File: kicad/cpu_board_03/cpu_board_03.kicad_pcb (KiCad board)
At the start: 2 copper layers, 99.1 x 94.2 mm, 62 parts, among them J1 DIN41612_02x32_AC, J11 Conn_01x09, J2 Clock, J6 Conn_01x02_Socket, J9 Ram1 Enable, SW1 SW_Reset, SW2 SW_PWR, U1 W65C02SxP, U10 74HC245, U13 74AHC1G32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

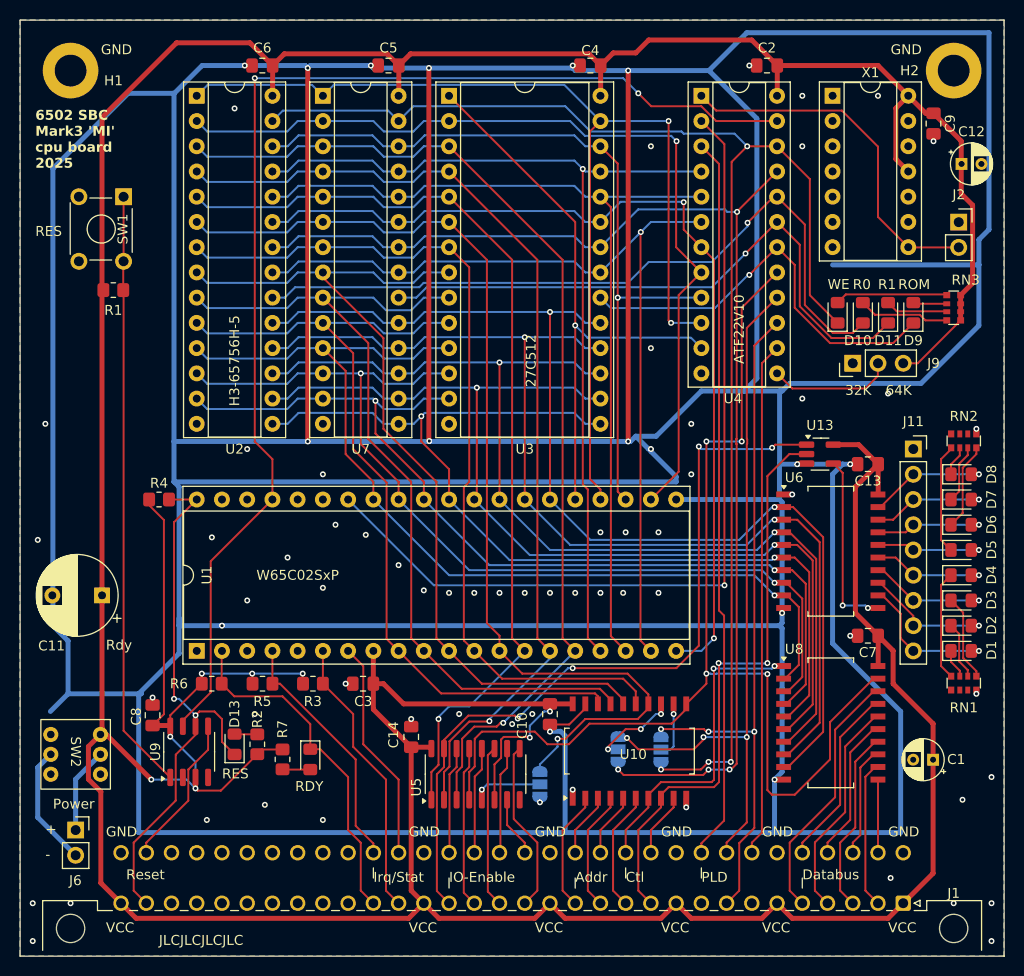
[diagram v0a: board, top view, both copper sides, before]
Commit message: uodate bus ow/wr signals
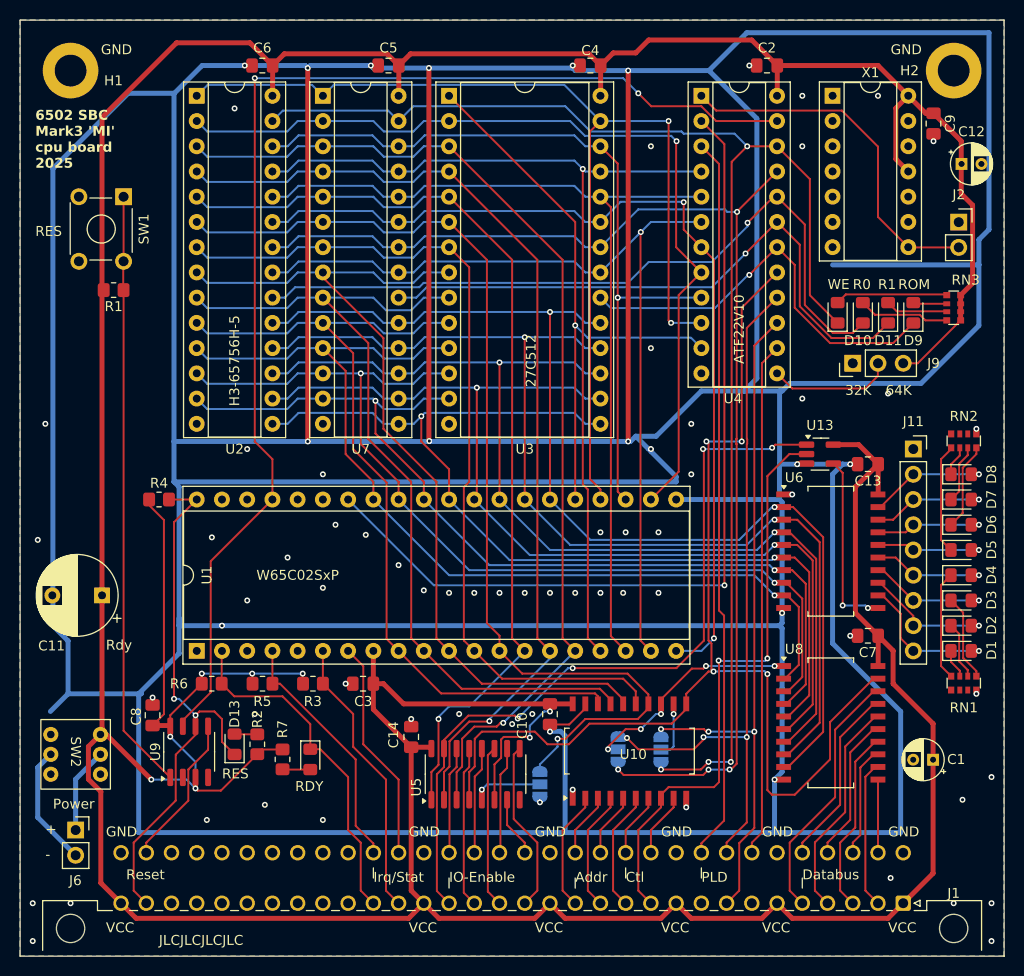
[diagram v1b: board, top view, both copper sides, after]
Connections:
- net Net-(JP2-C) renamed /~{BUS_WR}
- JP1 pad 2: Net-(JP1-C) -> /~{BUS_RD}
- U10 pad 13: Net-(JP1-C) -> /~{BUS_RD}
- U8 pad 1: /~{IO_RD} -> /~{BUS_RD}
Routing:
- net /~{IO_RD}: track 32.4 -> 6.43 mm, vias 2 -> 0
- net /~{BUS_RD}: track 0.00 -> 23.2 mm, vias 0 -> 5
- net Net-(JP1-C): track 8.99 -> 0.00 mm, vias 3 -> 0
- net /~{IOEN_00_GPIO0}: track 78.2 -> 77.7 mm

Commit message: optimized routing
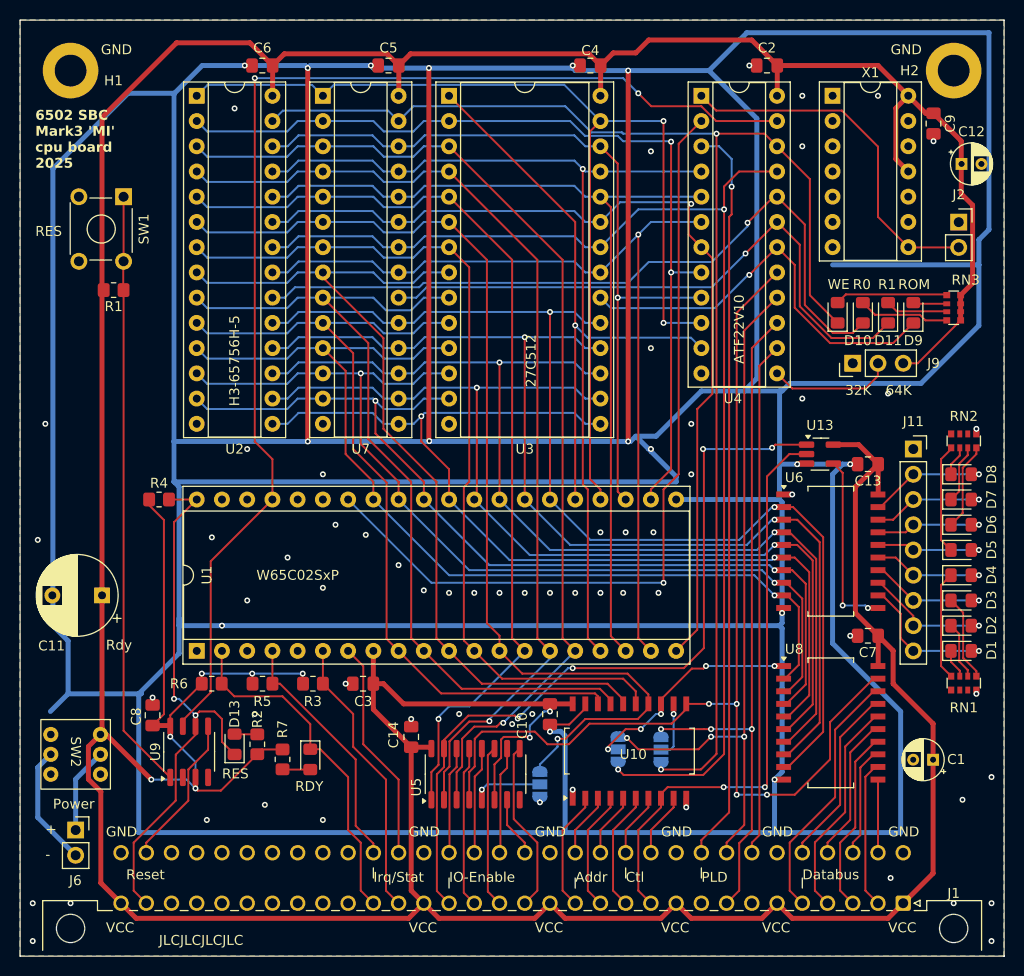
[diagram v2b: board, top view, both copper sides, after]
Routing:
- net /R/~{W}: track 89.2 -> 83.3 mm
- net /~{IO_SEL}: track 116.3 -> 111.1 mm
- net /PLD_I1: track 73.0 -> 74.7 mm, vias 0 -> 1
- net /~{QWE}: track 145.0 -> 143.7 mm, vias 4 -> 2
- net /A11: track 93.6 -> 92.5 mm, vias 2 -> 1
- net /~{OE}: track 125.0 -> 124.5 mm, vias 4 -> 2
- net /A12: track 90.1 -> 90.3 mm, vias 1 -> 2

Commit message: optimize routing / grounding
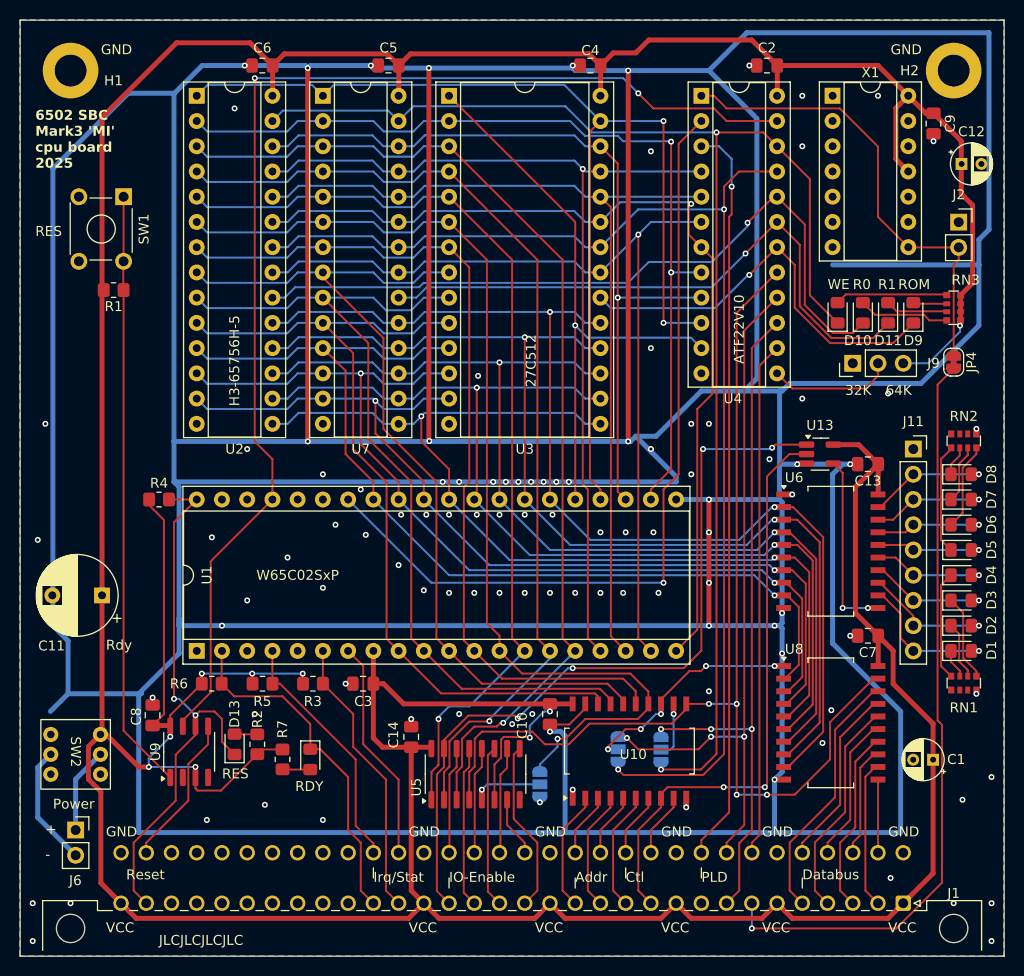
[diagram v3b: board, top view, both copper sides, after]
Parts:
- added JP4: SolderJumper_2_Bridged, Jumper:SolderJumper-2_P1.3mm_Bridged_RoundedPad1.0x1.5mm, F.Cu at (127.0, 47.1)
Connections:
- J1 pad a7: unconnected-(J1-Pin_a7-Pada7) -> Net-(J1-Pin_a7)
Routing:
- net Net-(J1-Pin_a7): track 0.00 -> 76.2 mm, vias 0 -> 1
- net GND: track 847.7 -> 860.4 mm, vias 78 -> 107
- net /CLOCK: track 36.4 -> 47.5 mm
- net VCC: track 512.2 -> 512.7 mm, vias 8 -> 9

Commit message: add GND testpoints
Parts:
- added TP1: TestPoint, TestPoint:TestPoint_Loop_D1.80mm_Drill1.0mm_Beaded, F.Cu at (112.8, 47.0)
- added TP2: TestPoint, TestPoint:TestPoint_Loop_D1.80mm_Drill1.0mm_Beaded, F.Cu at (97.8, 17.8)
- added TP3: TestPoint, TestPoint:TestPoint_Loop_D1.80mm_Drill1.0mm_Beaded, F.Cu at (61.0, 57.4)
- added TP4: TestPoint, TestPoint:TestPoint_Loop_D1.80mm_Drill1.0mm_Beaded, F.Cu at (57.4, 91.7)
- added TP5: TestPoint, TestPoint:TestPoint_Loop_D1.80mm_Drill1.0mm_Beaded, F.Cu at (122.2, 91.4)
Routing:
- net GND: track 860.4 -> 849.9 mm, vias 107 -> 106

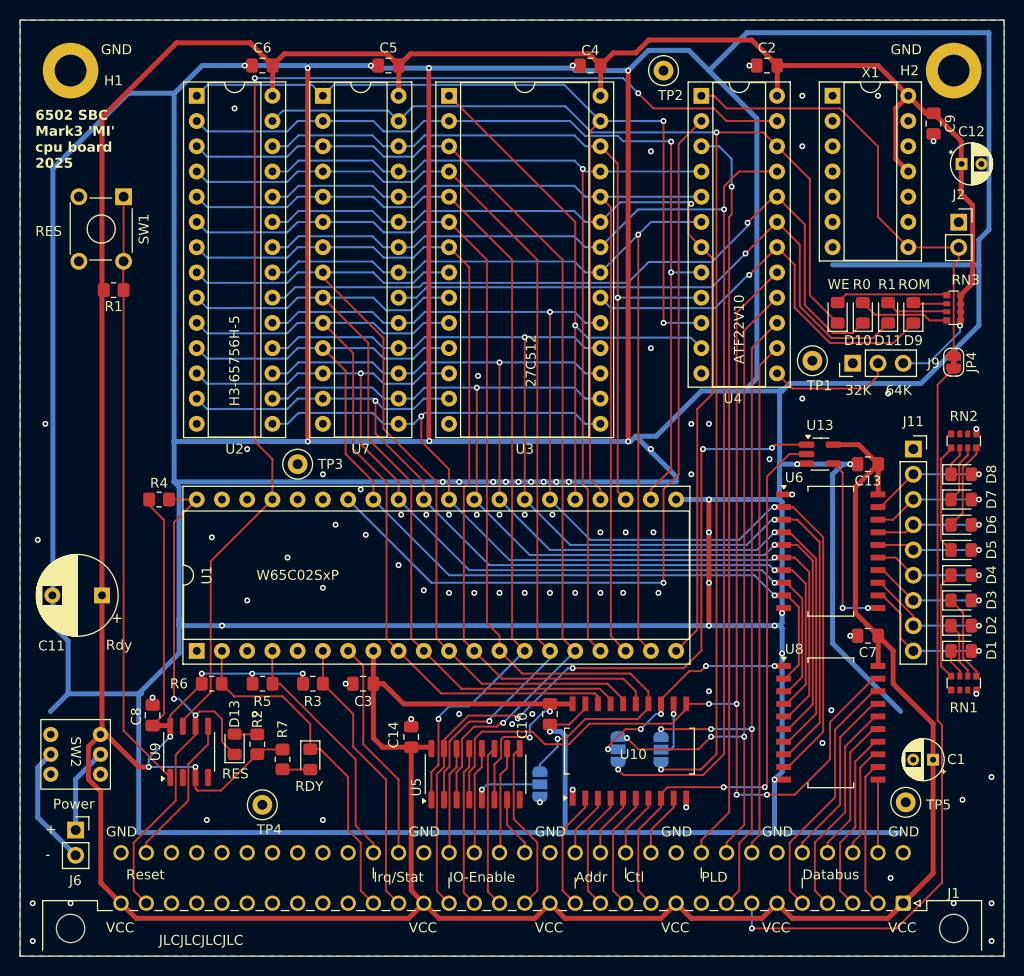
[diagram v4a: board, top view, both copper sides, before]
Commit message: us RN for status pullups
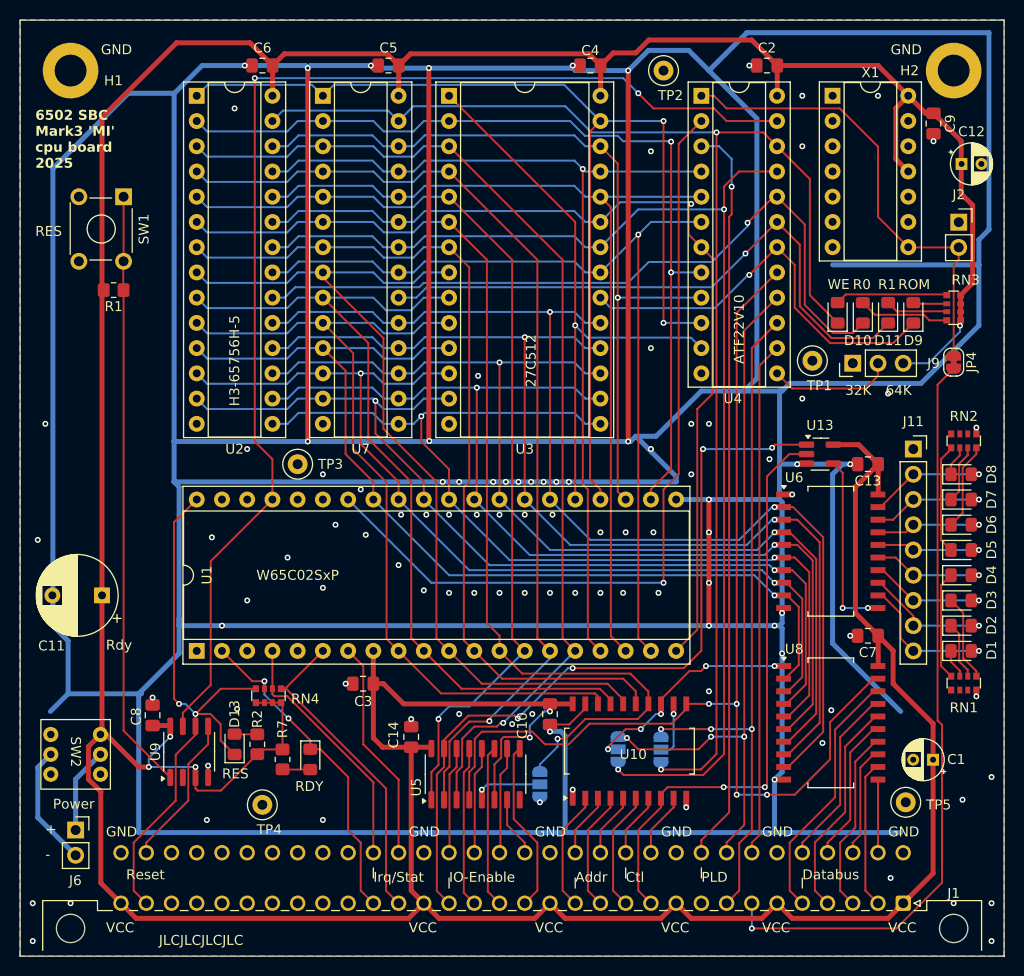
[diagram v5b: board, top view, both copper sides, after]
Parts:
- removed R3, R4, R5, R6: 10K, Resistor_SMD:R_0805_2012Metric_Pad1.20x1.40mm_HandSolder
- added RN4: R_Pack04, Resistor_SMD:R_Array_Convex_4x0612, F.Cu at (58.0, 80.7)
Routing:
- net VCC: track 512.7 -> 477.3 mm, vias 9 -> 6
- net /~{RES}: track 55.9 -> 60.0 mm
- net /~{NMI}: track 28.6 -> 32.6 mm
- net /RDY: track 35.2 -> 33.8 mm, vias 0 -> 2
- net GND: track 849.9 -> 850.3 mm, vias 106 -> 107

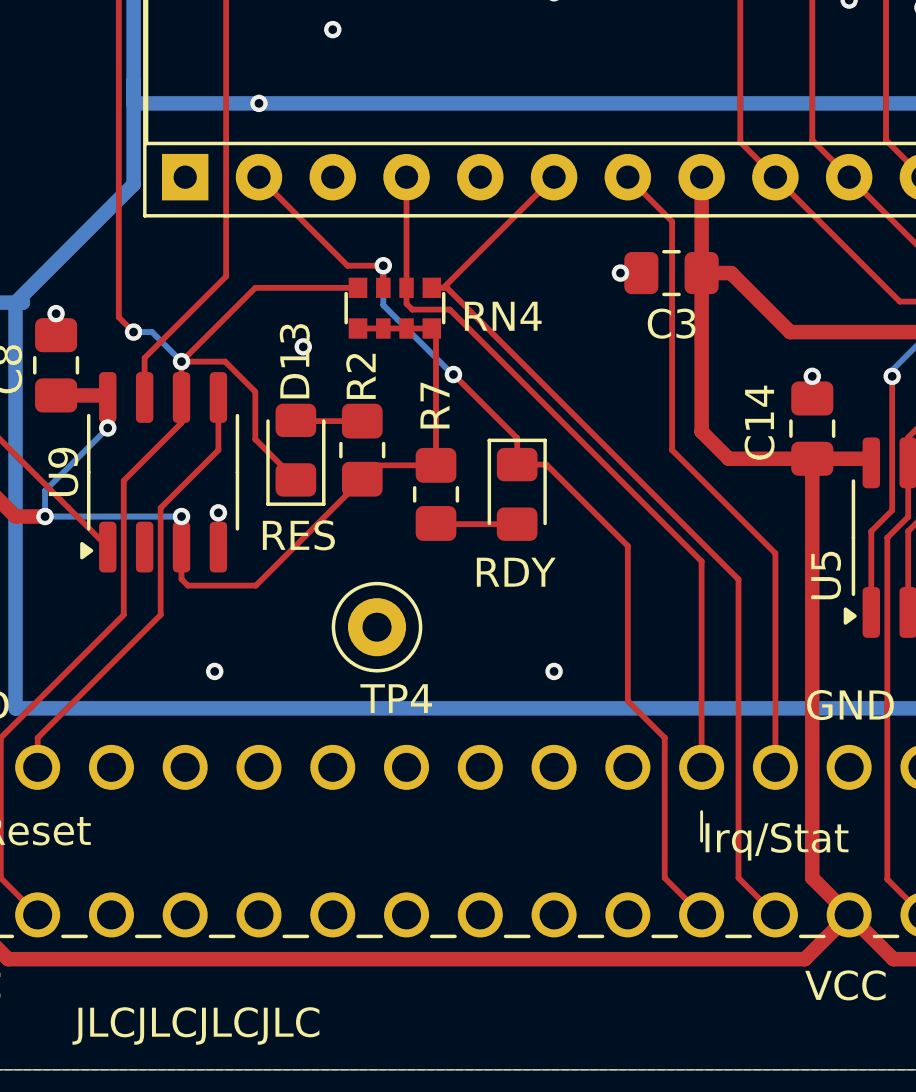
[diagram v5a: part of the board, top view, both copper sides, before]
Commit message: fiddle around with led placement
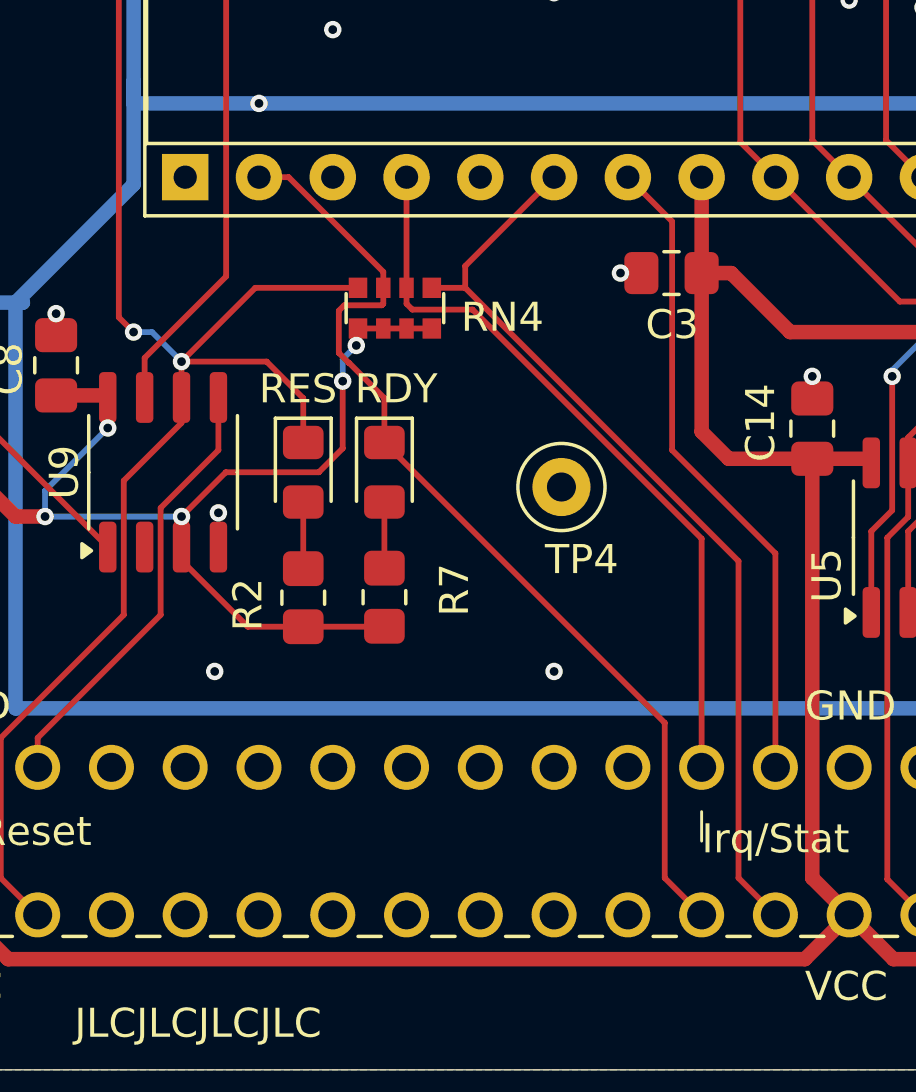
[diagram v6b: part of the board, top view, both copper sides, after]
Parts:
- moved TP4 7.98 mm to (63.8, 86.9)
- moved R2 5.47 mm to (54.9, 90.7)
- moved D14 4.64 mm to (57.7, 86.4)
- moved R7 3.96 mm to (57.7, 90.7), turned to 90 degrees
- moved D13 0.80 mm to (54.9, 86.4), turned to -90 degrees
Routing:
- net VCC: track 477.3 -> 480.3 mm, vias 6 -> 8
- net /RDY: track 33.8 -> 34.3 mm, vias 2 -> 0
- net Net-(D14-A): track 2.80 -> 2.28 mm
- net GND: vias 107 -> 106
